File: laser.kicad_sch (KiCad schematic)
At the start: 3 parts

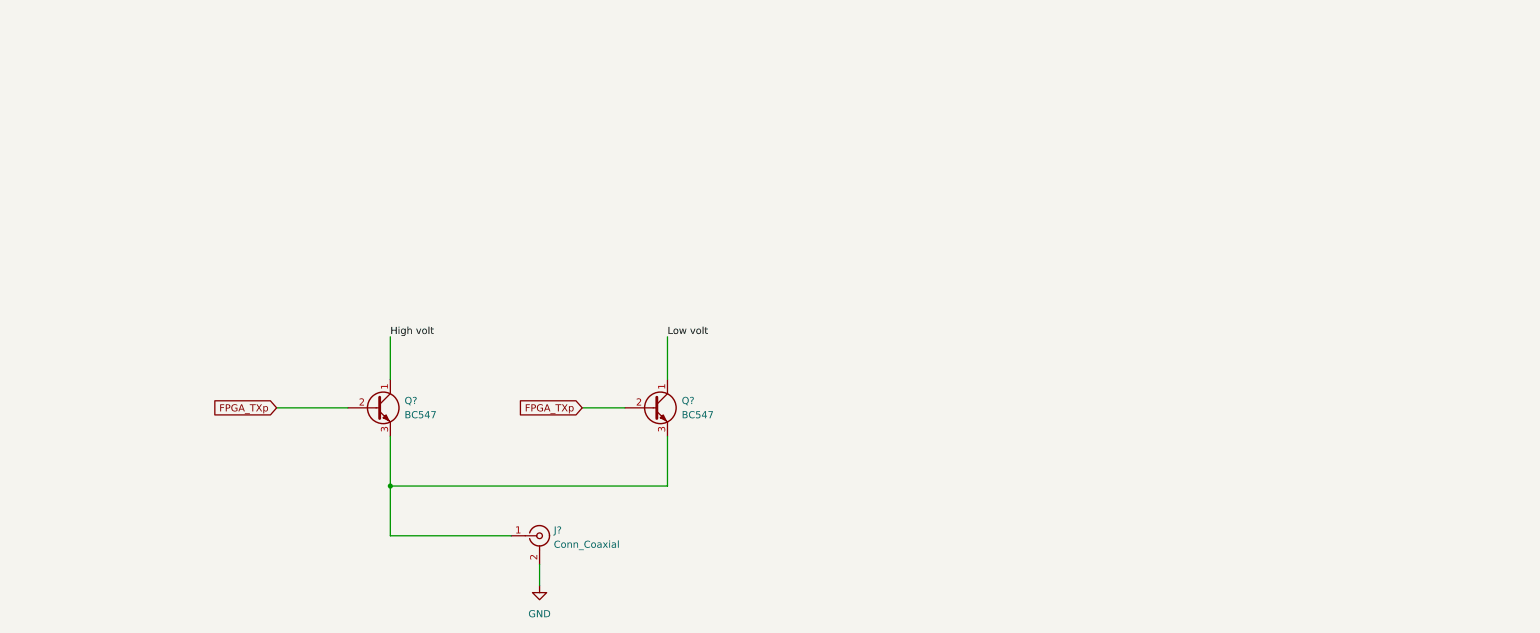
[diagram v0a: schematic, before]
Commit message: added start of vreg for laser drivers
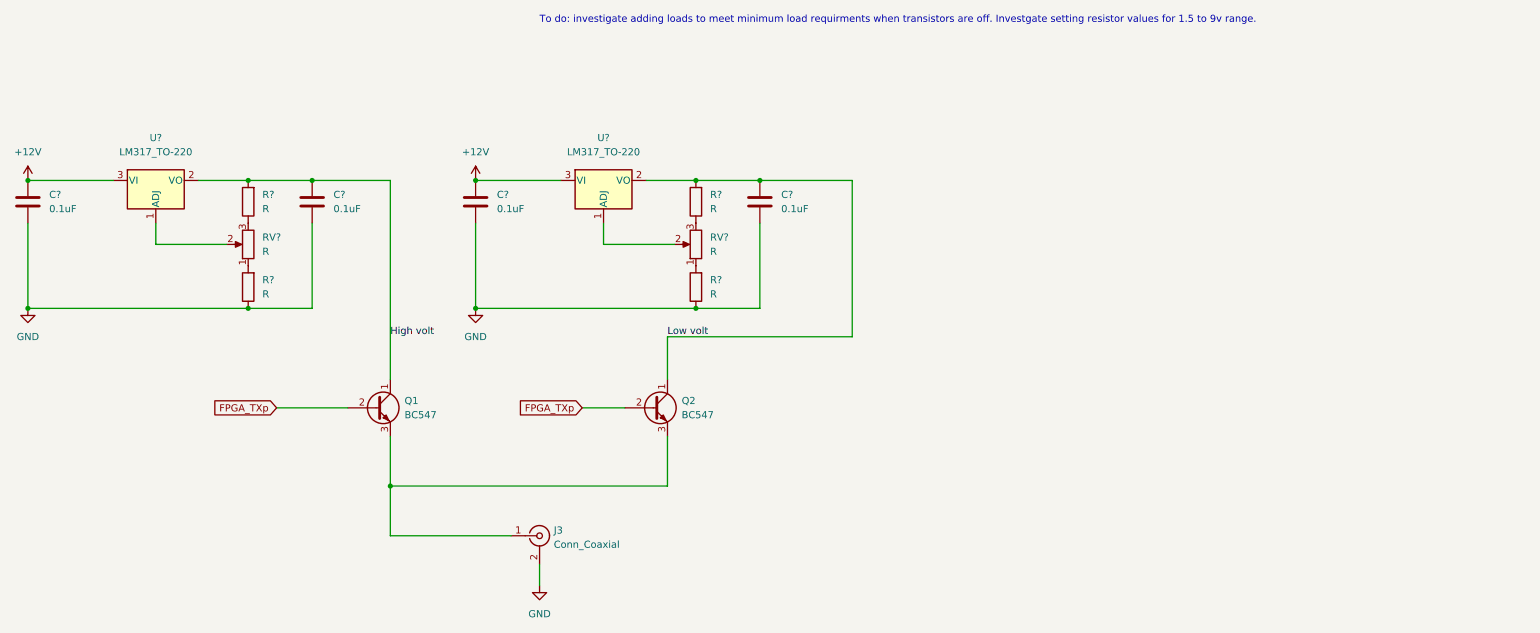
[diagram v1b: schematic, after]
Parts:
- added C? (x4): 0.1uF, symbol Device:C
- added R? (x4): R, symbol Device:R
- added RV? (x2): R, symbol Device:R_Potentiometer
- added U? (x2): LM317_TO-220, Package_TO_SOT_THT:TO-220-3_Vertical, symbol Regulator_Linear:LM317_TO-220
- gave numbers to parts that had none: 3
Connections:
- net GND: now also C?.2, C?.2, C?.2, C?.2, R?.1, R?.1
- net High volt: now also C?.1, R?.2, U?.2 (VO)
- net Low volt: now also C?.1, R?.2, U?.2 (VO)
- new net: RV?.2, U?.1 (ADJ) (x2)
- new net: R?.1, RV?.3 (x2)
- new net: R?.2, RV?.1 (x2)
- new net +12V: C?.1, C?.1, U?.3 (VI), U?.3 (VI)
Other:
- note added: "To do: investigate adding loads to meet minimum load requirments when transistors are off. Investgate setting resistor values for 1.5 to 9v range."

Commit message: change laser vrm design
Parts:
- removed C? (x2): 0.1uF, symbol Device:C
- removed R? (x3): R, symbol Device:R
- removed RV?: R, symbol Device:R_Potentiometer
- removed U?: LM317_TO-220, Package_TO_SOT_THT:TO-220-3_Vertical, symbol Regulator_Linear:LM317_TO-220
- added C? (x2): 0.1uF, symbol Device:C
- added R? (x3): R, symbol Device:R
- added RV?: R, symbol Device:R_Potentiometer
- added U?: LM317_TO-220, Package_TO_SOT_THT:TO-220-3_Vertical, symbol Regulator_Linear:LM317_TO-220
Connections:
- net +12V: now also C?.1, U?.3 (VI)
- net GND: now also C?.2, C?.2, R?.1, R?.1
- net Low volt: now also C?.1, R?.2, U?.2 (VO)
- net at U?.1 (ADJ): now also RV?.1, R?.2; no longer RV?.2
- net at R?.1: now also RV?.2; no longer RV?.3
- new net: R?.1, RV?.2
- new net: R?.2, RV?.1, U?.1 (ADJ)
- no-connect marks 0 -> 2
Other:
- moved on the sheet: Q2, RV?

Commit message: Add footprints to SMA connectors and FPGA
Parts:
- J3: footprint (none) -> Connector_Coaxial:SMA_Amphenol_901-144_Vertical
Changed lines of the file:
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@@
       (effects (font (size 1.27 1.27)) (justify left))
     )
-    (property "Footprint" "" (id 2) (at 132.08 110.49 0)
+    (property "Footprint" "Connector_Coaxial:SMA_Amphenol_901-144_Vertical" (id 2) (at 132.08 110.49 0)
       (effects (font (size 1.27 1.27)) hide)
     )

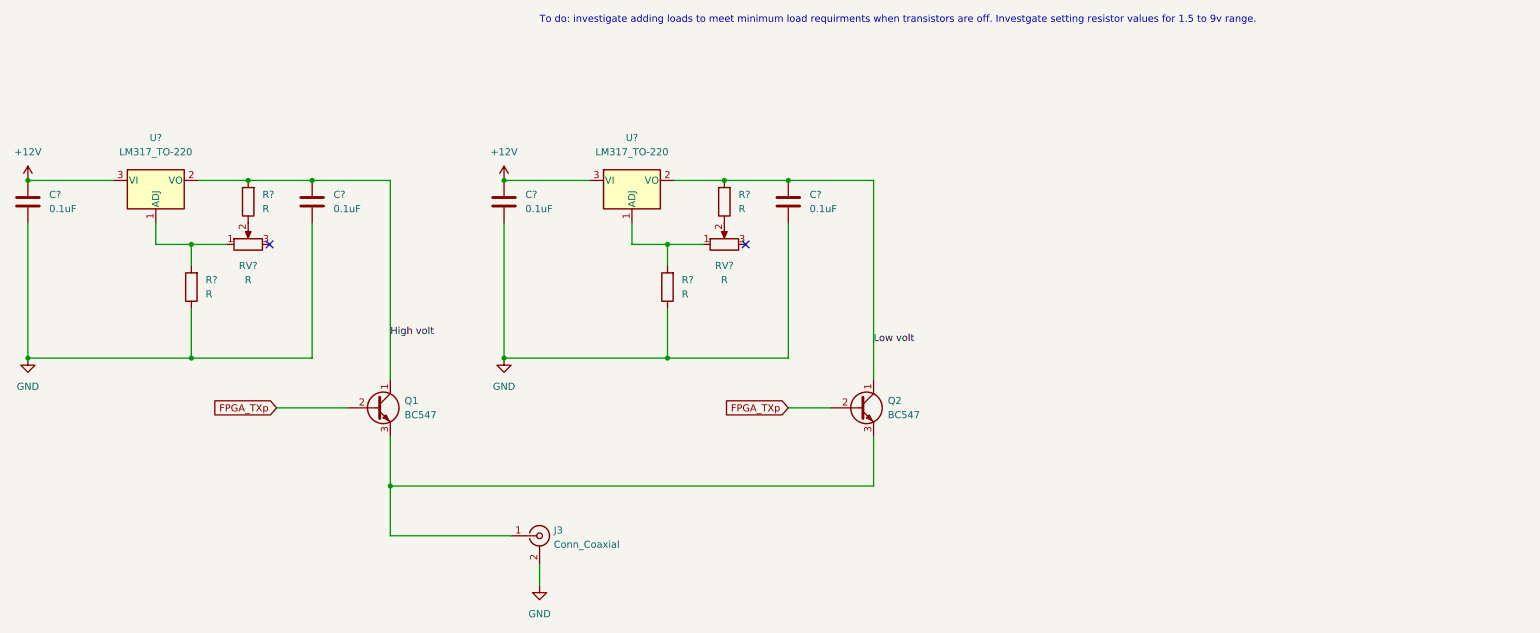
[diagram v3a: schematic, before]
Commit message: Assign footprints to ICs
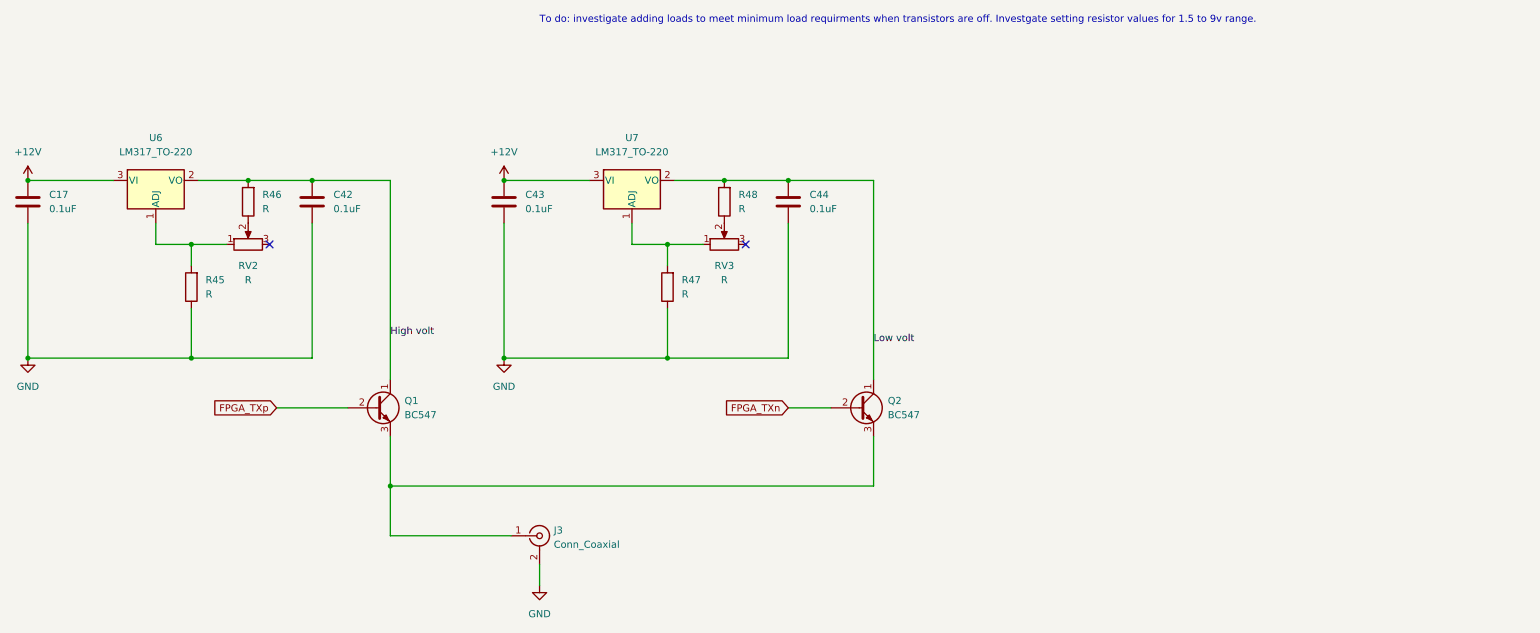
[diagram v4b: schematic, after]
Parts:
- gave numbers to parts that had none: 12
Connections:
- net FPGA_TXp: no longer Q2.2 (B)
- new net FPGA_TXn: Q2.2 (B)
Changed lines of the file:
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@@
   (junction (at 69.85 78.74) (diameter 0) (color 0 0 0 0)
   )
+  (junction (at 40.64 78.74) (diameter 0) (color 0 0 0 0)
+  )
+  (junction (at 40.64 46.99) (diameter 0) (color 0 0 0 0)
+  )
+  (junction (at 91.44 46.99) (diameter 0) (color 0 0 0 0)
+  )
+  (junction (at 176.53 46.99) (diameter 0) (color 0 0 0 0)
+  )
+  (junction (at 154.94 78.74) (diameter 0) (color 0 0 0 0)
+  )
+  (junction (at 69.85 58.42) (diameter 0) (color 0 0 0 0)
+  )
+  (junction (at 165.1 46.99) (diameter 0) (color 0 0 0 0)
+  )
   (junction (at 154.94 58.42) (diameter 0) (color 0 0 0 0)
-  )
-  (junction (at 40.64 78.74) (diameter 0) (color 0 0 0 0)
-  )
-  (junction (at 40.64 46.99) (diameter 0) (color 0 0 0 0)
-  )
-  (junction (at 91.44 46.99) (diameter 0) (color 0 0 0 0)
-  )
-  (junction (at 176.53 46.99) (diameter 0) (color 0 0 0 0)
-  )
-  (junction (at 154.94 78.74) (diameter 0) (color 0 0 0 0)
-  )
-  (junction (at 69.85 58.42) (diameter 0) (color 0 0 0 0)
-  )
-  (junction (at 165.1 46.99) (diameter 0) (color 0 0 0 0)
   )
   (junction (at 125.73 78.74) (diameter 0) (color 0 0 0 0)
@@
     (stroke (width 0) (type default) (color 0 0 0 0))
   )
-  (wire (pts (xy 161.29 58.42) (xy 154.94 58.42))
-    (stroke (width 0) (type default) (color 0 0 0 0))
-  )
   (wire (pts (xy 91.44 46.99) (xy 105.41 46.99))
     (stroke (width 0) (type default) (color 0 0 0 0))
   )
-  (wire (pts (xy 154.94 58.42) (xy 148.59 58.42))
+  (wire (pts (xy 154.94 58.42) (xy 154.94 62.23))
     (stroke (width 0) (type default) (color 0 0 0 0))
   )
@@
     (stroke (width 0) (type default) (color 0 0 0 0))
   )
-  (wire (pts (xy 154.94 58.42) (xy 154.94 62.23))
-    (stroke (width 0) (type default) (color 0 0 0 0))
-  )
   (wire (pts (xy 125.73 78.74) (xy 154.94 78.74))
     (stroke (width 0) (type default) (color 0 0 0 0))
@@
     (stroke (width 0) (type default) (color 0 0 0 0))
   )
+  (wire (pts (xy 148.59 58.42) (xy 154.94 58.42))
+    (stroke (width 0) (type default) (color 0 0 0 0))
+  )
   (wire (pts (xy 176.53 54.61) (xy 176.53 78.74))
     (stroke (width 0) (type default) (color 0 0 0 0))
@@
     (stroke (width 0) (type default) (color 0 0 0 0))
   )
-  (wire (pts (xy 148.59 58.42) (xy 148.59 54.61))
-    (stroke (width 0) (type default) (color 0 0 0 0))
-  )
   (wire (pts (xy 105.41 46.99) (xy 105.41 82.55))
     (stroke (width 0) (type default) (color 0 0 0 0))
@@
     (stroke (width 0) (type default) (color 0 0 0 0))
   )
+  (wire (pts (xy 154.94 58.42) (xy 161.29 58.42))
+    (stroke (width 0) (type default) (color 0 0 0 0))
+  )
   (wire (pts (xy 176.53 87.63) (xy 184.15 87.63))
     (stroke (width 0) (type default) (color 0 0 0 0))
   )
   (wire (pts (xy 69.85 69.85) (xy 69.85 78.74))
+    (stroke (width 0) (type default) (color 0 0 0 0))
+  )
+  (wire (pts (xy 148.59 54.61) (xy 148.59 58.42))
     (stroke (width 0) (type default) (color 0 0 0 0))
   )
@@
     )
   )
-  (global_label "FPGA_TXp" (shape input) (at 176.53 87.63 180) (fields_autoplaced)
+  (global_label "FPGA_TXn" (shape input) (at 176.53 87.63 180) (fields_autoplaced)
     (effects (font (size 1.27 1.27)) (justify right))
     (property "Intersheet References" "${INTERSHEET_REFS}" (id 0) (at 165.1059 87.5506 0)
@@
   (symbol (lib_id "Device:C") (at 176.53 50.8 0) (unit 1)
     (in_bom yes) (on_board yes) (fields_autoplaced)
-    (property "Reference" "C?" (id 0) (at 180.34 49.5299 0)
+    (property "Reference" "C44" (id 0) (at 180.34 49.5299 0)
       (effects (font (size 1.27 1.27)) (justify left))
     )
@@
   (symbol (lib_id "Regulator_Linear:LM317_TO-220") (at 63.5 46.99 0) (unit 1)
     (in_bom yes) (on_board yes) (fields_autoplaced)
-    (property "Reference" "U?" (id 0) (at 63.5 39.37 0))
+    (property "Reference" "U6" (id 0) (at 63.5 39.37 0))
     (property "Value" "LM317_TO-220" (id 1) (at 63.5 41.91 0))
     (property "Footprint" "Package_TO_SOT_THT:TO-220-3_Vertical" (id 2) (at 63.5 40.64 0)
@@
   (symbol (lib_id "power:+12V") (at 40.64 46.99 0) (unit 1)
     (in_bom yes) (on_board yes) (fields_autoplaced)
-    (property "Reference" "#PWR?" (id 0) (at 40.64 50.8 0)
+    (property "Reference" "#PWR0104" (id 0) (at 40.64 50.8 0)
       (effects (font (size 1.27 1.27)) hide)
     )
@@
   (symbol (lib_id "Device:C") (at 125.73 50.8 0) (unit 1)
     (in_bom yes) (on_board yes) (fields_autoplaced)
-    (property "Reference" "C?" (id 0) (at 129.54 49.5299 0)
+    (property "Reference" "C43" (id 0) (at 129.54 49.5299 0)
       (effects (font (size 1.27 1.27)) (justify left))
     )
@@
   (symbol (lib_id "Device:C") (at 91.44 50.8 0) (unit 1)
     (in_bom yes) (on_board yes) (fields_autoplaced)
-    (property "Reference" "C?" (id 0) (at 95.25 49.5299 0)
+    (property "Reference" "C42" (id 0) (at 95.25 49.5299 0)
       (effects (font (size 1.27 1.27)) (justify left))
     )
@@
   (symbol (lib_id "Device:R") (at 69.85 66.04 180) (unit 1)
     (in_bom yes) (on_board yes) (fields_autoplaced)
-    (property "Reference" "R?" (id 0) (at 72.39 64.7699 0)
+    (property "Reference" "R45" (id 0) (at 72.39 64.7699 0)
       (effects (font (size 1.27 1.27)) (justify right))
     )
@@
   (symbol (lib_id "Device:R") (at 80.01 50.8 180) (unit 1)
     (in_bom yes) (on_board yes) (fields_autoplaced)
-    (property "Reference" "R?" (id 0) (at 82.55 49.5299 0)
+    (property "Reference" "R46" (id 0) (at 82.55 49.5299 0)
       (effects (font (size 1.27 1.27)) (justify right))
     )
@@
   (symbol (lib_id "Device:R") (at 165.1 50.8 180) (unit 1)
     (in_bom yes) (on_board yes) (fields_autoplaced)
-    (property "Reference" "R?" (id 0) (at 167.64 49.5299 0)
+    (property "Reference" "R48" (id 0) (at 167.64 49.5299 0)
       (effects (font (size 1.27 1.27)) (justify right))
     )
@@
   (symbol (lib_id "Regulator_Linear:LM317_TO-220") (at 148.59 46.99 0) (unit 1)
     (in_bom yes) (on_board yes) (fields_autoplaced)
-    (property "Reference" "U?" (id 0) (at 148.59 39.37 0))
+    (property "Reference" "U7" (id 0) (at 148.59 39.37 0))
     (property "Value" "LM317_TO-220" (id 1) (at 148.59 41.91 0))
     (property "Footprint" "Package_TO_SOT_THT:TO-220-3_Vertical" (id 2) (at 148.59 40.64 0)
@@
   (symbol (lib_id "Device:R_Potentiometer") (at 80.01 58.42 90) (unit 1)
     (in_bom yes) (on_board yes)
-    (property "Reference" "RV?" (id 0) (at 80.01 62.23 90))
+    (property "Reference" "RV2" (id 0) (at 80.01 62.23 90))
     (property "Value" "R" (id 1) (at 80.01 64.77 90))
     (property "Footprint" "" (id 2) (at 80.01 58.42 0)
@@
   (symbol (lib_id "Device:C") (at 40.64 50.8 0) (unit 1)
     (in_bom yes) (on_board yes) (fields_autoplaced)
-    (property "Reference" "C?" (id 0) (at 44.45 49.5299 0)
+    (property "Reference" "C17" (id 0) (at 44.45 49.5299 0)
       (effects (font (size 1.27 1.27)) (justify left))
     )
@@
   (symbol (lib_id "Device:R_Potentiometer") (at 165.1 58.42 90) (unit 1)
     (in_bom yes) (on_board yes)
-    (property "Reference" "RV?" (id 0) (at 165.1 62.23 90))
+    (property "Reference" "RV3" (id 0) (at 165.1 62.23 90))
     (property "Value" "R" (id 1) (at 165.1 64.77 90))
     (property "Footprint" "" (id 2) (at 165.1 58.42 0)
@@
   (symbol (lib_id "power:+12V") (at 125.73 46.99 0) (unit 1)
     (in_bom yes) (on_board yes) (fields_autoplaced)
-    (property "Reference" "#PWR?" (id 0) (at 125.73 50.8 0)
+    (property "Reference" "#PWR0103" (id 0) (at 125.73 50.8 0)
       (effects (font (size 1.27 1.27)) hide)
     )
@@
   (symbol (lib_id "power:GND") (at 125.73 78.74 0) (unit 1)
     (in_bom yes) (on_board yes) (fields_autoplaced)
-    (property "Reference" "#PWR?" (id 0) (at 125.73 85.09 0)
+    (property "Reference" "#PWR0102" (id 0) (at 125.73 85.09 0)
       (effects (font (size 1.27 1.27)) hide)
     )
@@
   (symbol (lib_id "power:GND") (at 40.64 78.74 0) (unit 1)
     (in_bom yes) (on_board yes) (fields_autoplaced)
-    (property "Reference" "#PWR?" (id 0) (at 40.64 85.09 0)
+    (property "Reference" "#PWR0105" (id 0) (at 40.64 85.09 0)
       (effects (font (size 1.27 1.27)) hide)
     )
@@
   (symbol (lib_id "Device:R") (at 154.94 66.04 180) (unit 1)
     (in_bom yes) (on_board yes) (fields_autoplaced)
-    (property "Reference" "R?" (id 0) (at 157.48 64.7699 0)
-      (effects (font (size 1.27 1.27)) (justify right))
-    )
+    (property "Reference" "R47" (id 0) (at 157.48 64.7699 0)
+      (effects (font (size 1.27 1.27)) (justify right))
+    )

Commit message: Resistor and cap footprints (except the ones the store cupboard doesn't have)
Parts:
- C17, C42, C43, C44: footprint (none) -> Capacitor_SMD:C_0805_2012Metric_Pad1.18x1.45mm_HandSolder
- R45, R46, R47, R48: footprint (none) -> Resistor_SMD:R_0805_2012Metric_Pad1.20x1.40mm_HandSolder
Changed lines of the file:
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@@
       (effects (font (size 1.27 1.27)) (justify left))
     )
-    (property "Footprint" "" (id 2) (at 177.4952 54.61 0)
+    (property "Footprint" "Capacitor_SMD:C_0805_2012Metric_Pad1.18x1.45mm_HandSolder" (id 2) (at 177.4952 54.61 0)
       (effects (font (size 1.27 1.27)) hide)
     )
@@
       (effects (font (size 1.27 1.27)) (justify left))
     )
-    (property "Footprint" "" (id 2) (at 126.6952 54.61 0)
+    (property "Footprint" "Capacitor_SMD:C_0805_2012Metric_Pad1.18x1.45mm_HandSolder" (id 2) (at 126.6952 54.61 0)
       (effects (font (size 1.27 1.27)) hide)
     )
@@
       (effects (font (size 1.27 1.27)) (justify left))
     )
-    (property "Footprint" "" (id 2) (at 92.4052 54.61 0)
+    (property "Footprint" "Capacitor_SMD:C_0805_2012Metric_Pad1.18x1.45mm_HandSolder" (id 2) (at 92.4052 54.61 0)
       (effects (font (size 1.27 1.27)) hide)
     )
@@
       (effects (font (size 1.27 1.27)) (justify right))
     )
-    (property "Footprint" "" (id 2) (at 71.628 66.04 90)
+    (property "Footprint" "Resistor_SMD:R_0805_2012Metric_Pad1.20x1.40mm_HandSolder" (id 2) (at 71.628 66.04 90)
       (effects (font (size 1.27 1.27)) hide)
     )
@@
       (effects (font (size 1.27 1.27)) (justify right))
     )
-    (property "Footprint" "" (id 2) (at 81.788 50.8 90)
+    (property "Footprint" "Resistor_SMD:R_0805_2012Metric_Pad1.20x1.40mm_HandSolder" (id 2) (at 81.788 50.8 90)
       (effects (font (size 1.27 1.27)) hide)
     )
@@
       (effects (font (size 1.27 1.27)) (justify right))
     )
-    (property "Footprint" "" (id 2) (at 166.878 50.8 90)
+    (property "Footprint" "Resistor_SMD:R_0805_2012Metric_Pad1.20x1.40mm_HandSolder" (id 2) (at 166.878 50.8 90)
       (effects (font (size 1.27 1.27)) hide)
     )
@@
       (effects (font (size 1.27 1.27)) (justify left))
     )
-    (property "Footprint" "" (id 2) (at 41.6052 54.61 0)
+    (property "Footprint" "Capacitor_SMD:C_0805_2012Metric_Pad1.18x1.45mm_HandSolder" (id 2) (at 41.6052 54.61 0)
       (effects (font (size 1.27 1.27)) hide)
     )
@@
       (effects (font (size 1.27 1.27)) (justify right))
     )
-    (property "Footprint" "" (id 2) (at 156.718 66.04 90)
-      (effects (font (size 1.27 1.27)) hide)
-    )
+    (property "Footprint" "Resistor_SMD:R_0805_2012Metric_Pad1.20x1.40mm_HandSolder" (id 2) (at 156.718 66.04 90)
+      (effects (font (size 1.27 1.27)) hide)
+    )

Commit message: Assign footprints to everything bar inductors
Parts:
- RV2, RV3: footprint (none) -> Trimmer:T93YB104KT20
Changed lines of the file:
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@@
     (property "Reference" "RV2" (id 0) (at 80.01 62.23 90))
     (property "Value" "R" (id 1) (at 80.01 64.77 90))
-    (property "Footprint" "" (id 2) (at 80.01 58.42 0)
+    (property "Footprint" "Trimmer:T93YB104KT20" (id 2) (at 80.01 58.42 0)
       (effects (font (size 1.27 1.27)) hide)
     )
@@
     (property "Reference" "RV3" (id 0) (at 165.1 62.23 90))
     (property "Value" "R" (id 1) (at 165.1 64.77 90))
-    (property "Footprint" "" (id 2) (at 165.1 58.42 0)
+    (property "Footprint" "Trimmer:T93YB104KT20" (id 2) (at 165.1 58.42 0)
       (effects (font (size 1.27 1.27)) hide)
     )
